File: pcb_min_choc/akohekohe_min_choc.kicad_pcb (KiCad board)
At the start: 2 copper layers, 187.5 x 87.9 mm, 33 parts, among them U1 xiao

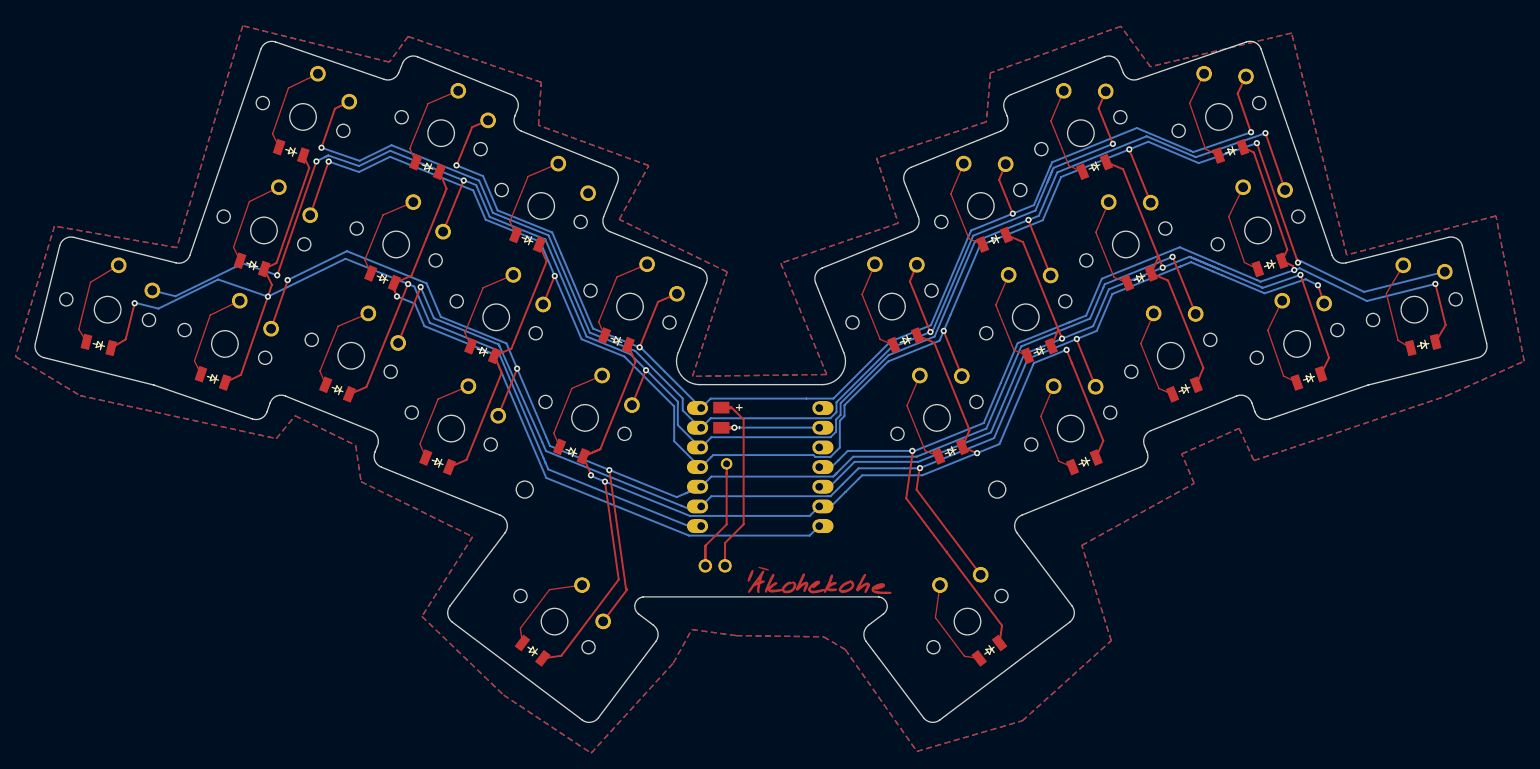
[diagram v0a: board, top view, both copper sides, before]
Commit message: ran DRC and fixed minspace
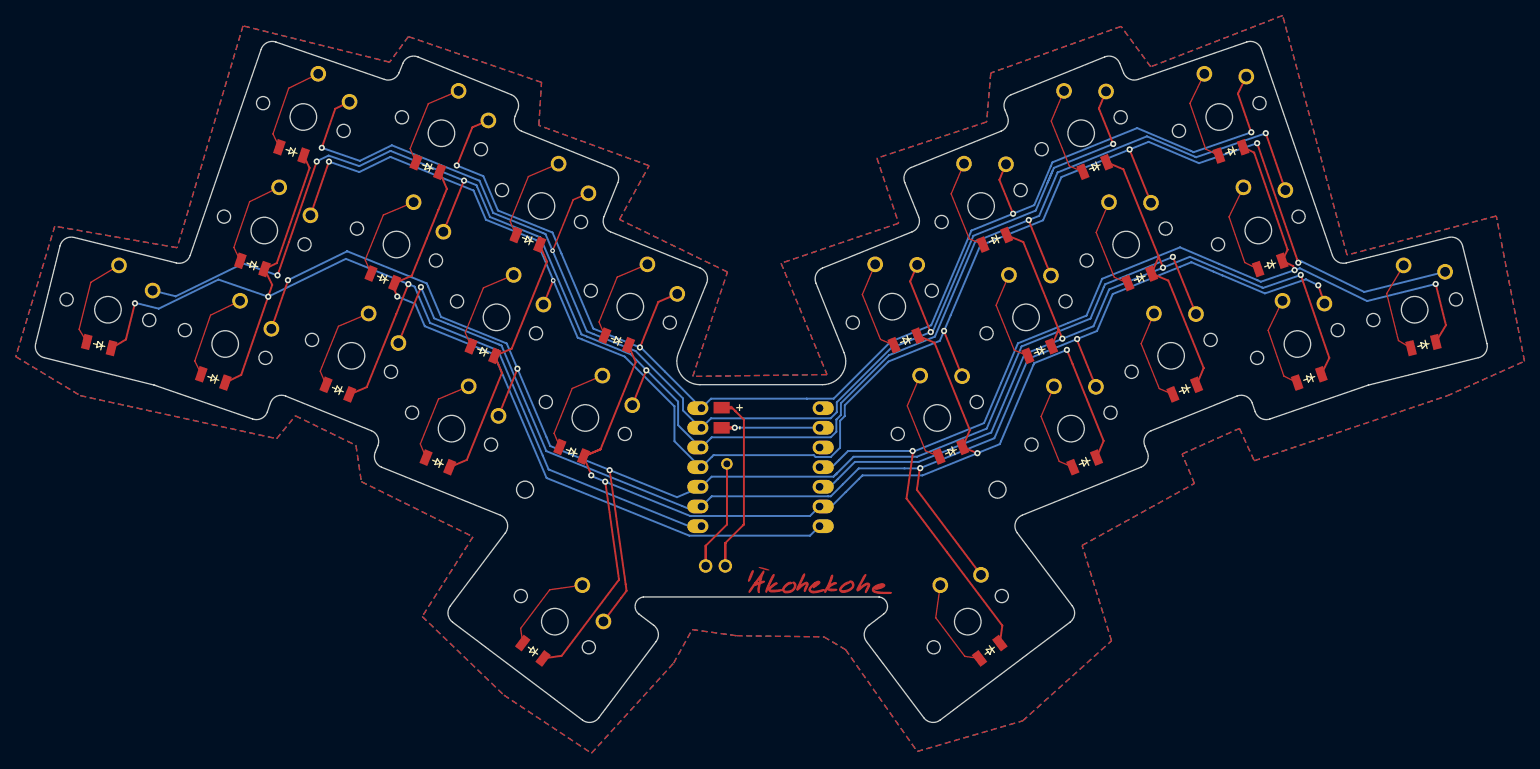
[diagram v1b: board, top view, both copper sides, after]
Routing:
- net P1: track 165.5 -> 174.6 mm, vias 3 -> 4
- net P9: track 149.2 -> 145.2 mm
- net P4: track 189.6 -> 187.3 mm
- net P3: track 227.2 -> 226.5 mm
- net P10: track 151.1 -> 150.6 mm
